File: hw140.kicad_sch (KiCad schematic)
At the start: 23 parts, among them Q1 NPN, Q2 PNP, Q4 NCE6075k, Q5 D4184

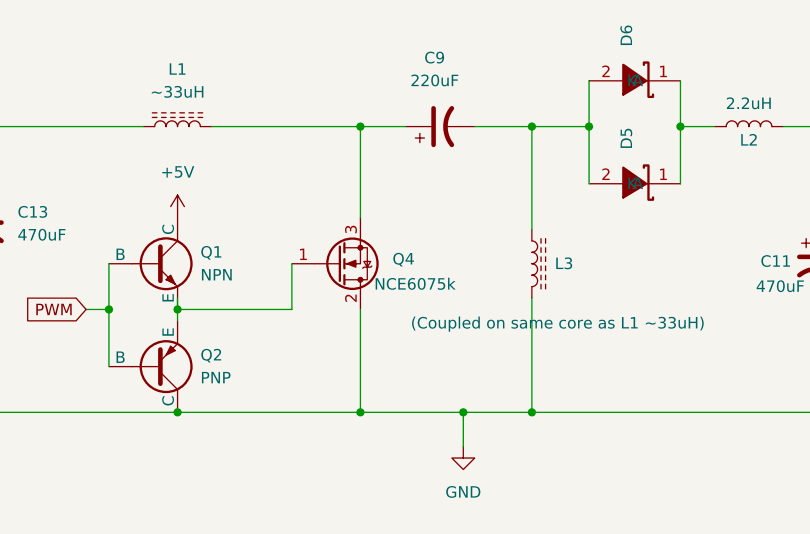
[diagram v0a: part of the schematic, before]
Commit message: Fix reversed MOSFET
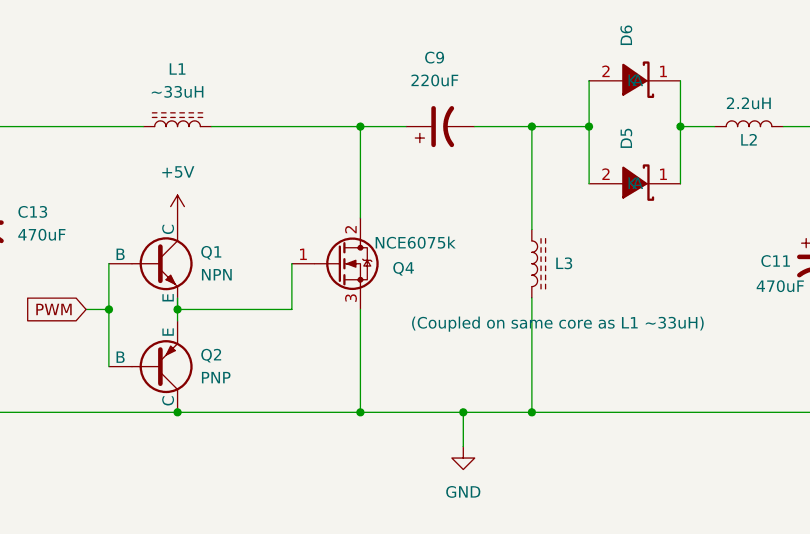
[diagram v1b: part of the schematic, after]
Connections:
- net GND: now also Q4.3 (S); no longer Q4.2 (D)
- net at C9.1, L1.2: now also Q4.2 (D); no longer Q4.3 (S)
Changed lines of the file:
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@@
 		(lib_id "Transistor_FET:IRLZ44N")
 		(at 133.35 91.44 0)
-		(mirror x)
 		(unit 1)
 		(exclude_from_sim no)
@@
 		(dnp no)
 		(property "Reference" "Q4"
-			(at 139.446 90.932 0)
+			(at 139.446 91.948 0)
 			(effects
 				(font
@@
 		)
 		(property "Value" "NCE6075k"
-			(at 137.414 93.726 0)
+			(at 137.414 89.154 0)
 			(effects
 				(font
@@
 		)
 		(property "Footprint" "Package_TO_SOT_SMD:TO-252-2"
-			(at 138.43 89.535 0)
+			(at 138.43 93.345 0)
 			(effects
 				(font
@@
 		)
 		(property "Datasheet" "https://www.lcsc.com/datasheet/C110912.pdf"
-			(at 138.43 87.63 0)
+			(at 138.43 95.25 0)
 			(effects
 				(font
@@
 		)
 		(instances
-			(project ""
+			(project "hw140"
 				(path "/475ab2b5-d626-4c42-995d-fb9fe70106f6"
 					(reference "Q4")
